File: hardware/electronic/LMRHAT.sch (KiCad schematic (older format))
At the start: 17 parts, among them J1 Speaker Connector, J2 Serial, J5 RPi Expansion Connector, U1 MAX98357AETE+T, U9 SPH0645LM4H-B

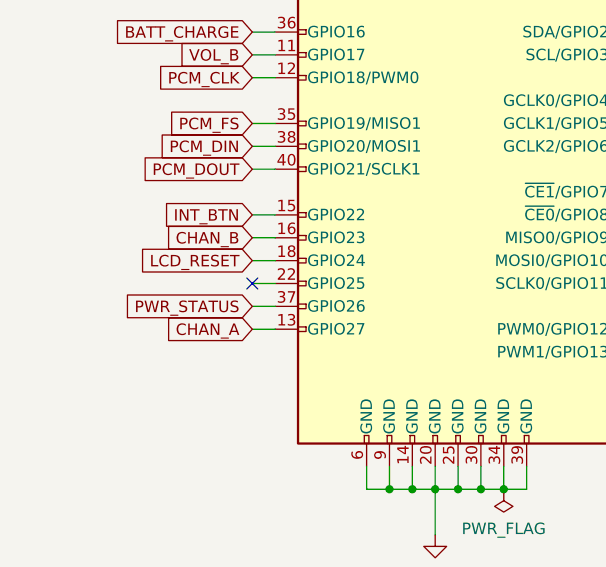
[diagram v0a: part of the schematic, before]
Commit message: Connected power switch to a GPIO and moved the layout for readability
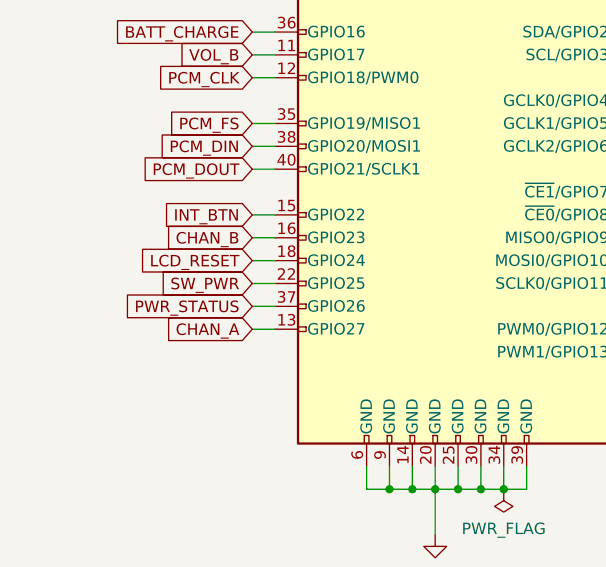
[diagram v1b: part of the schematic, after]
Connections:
- net SW_PWR: now reaches J5.22 (GPIO25)
- no-connect marks 7 -> 6
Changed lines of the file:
@@
 	6700 3500 6900 3500
 NoConn ~ 3500 3500
-NoConn ~ 1700 3200
 $Comp
 L power:PWR_FLAG #FLG0102
@@
 NoConn ~ 3500 2600
 NoConn ~ 3500 2500
+Text GLabel 1700 3200 0    50   Input ~ 0
+SW_PWR
 $EndSCHEMATC

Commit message: Rescued schematic symbols since LMRHAT.lib didn't get saved
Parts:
- MK1, MK2, MK4, MK5, MK6: symbol LMRHAT-rescue:Mounting_Hole-Mechanical -> LMRHAT-rescue:Mounting_Hole-Mechanical-LMRHAT-rescue
- U1: symbol LMRHAT:MAX98357AETE+T -> LMRHAT-rescue:MAX98357AETE+T-LMRHAT
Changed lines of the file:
@@
 $EndDescr
 $Comp
-L LMRHAT-rescue:Mounting_Hole-Mechanical MK1
+L LMRHAT-rescue:Mounting_Hole-Mechanical-LMRHAT-rescue MK1
 U 1 1 5834FB2E
 P 750 6050
@@
 $EndComp
 $Comp
-L LMRHAT-rescue:Mounting_Hole-Mechanical MK2
+L LMRHAT-rescue:Mounting_Hole-Mechanical-LMRHAT-rescue MK2
 U 1 1 5834FC19
 P 750 6250
@@
 $EndComp
 $Comp
-L LMRHAT-rescue:Mounting_Hole-Mechanical MK4
+L LMRHAT-rescue:Mounting_Hole-Mechanical-LMRHAT-rescue MK4
 U 1 1 5834FC4F
 P 1200 6250
@@
 	2300 4100 2400 4100
 $Comp
-L LMRHAT:GND #PWR0142
+L LMRHAT-rescue:GND-LMRHAT #PWR0142
 U 1 1 5C81337F
 P 2500 4300
@@
 Connection ~ 2800 1300
 $Comp
-L LMRHAT:+Vopt #PWR0143
+L LMRHAT-rescue:+Vopt-LMRHAT #PWR0143
 U 1 1 5C916BC8
 P 2400 1200
@@
 $EndComp
 $Comp
-L LMRHAT:+3.3V #PWR0144
+L LMRHAT-rescue:+3.3V-LMRHAT #PWR0144
 U 1 1 5C916CAE
 P 2800 1200
@@
 $EndComp
 $Comp
-L LMRHAT:GND #PWR0101
+L LMRHAT-rescue:GND-LMRHAT #PWR0101
 U 1 1 5C9E3D74
 P 4100 3200
@@
 $EndSheet
 $Comp
-L LMRHAT:MAX98357AETE+T U1
+L LMRHAT-rescue:MAX98357AETE+T-LMRHAT U1
 U 1 1 5C1DD312
 P 7650 2250
@@
 	7100 2500 7050 2500
 $Comp
-L LMRHAT:GND #PWR0102
+L LMRHAT-rescue:GND-LMRHAT #PWR0102
 U 1 1 5C1DD31D
 P 8300 2700
@@
 	6900 2100 7100 2100
 $Comp
-L LMRHAT:GND #PWR0103
+L LMRHAT-rescue:GND-LMRHAT #PWR0103
 U 1 1 5C1DD324
 P 6900 2200
@@
 Connection ~ 6500 2500
 $Comp
-L LMRHAT:GND #PWR0104
+L LMRHAT-rescue:GND-LMRHAT #PWR0104
 U 1 1 5C1DD345
 P 6500 2950
@@
 $EndComp
 $Comp
-L LMRHAT:GND #PWR0105
+L LMRHAT-rescue:GND-LMRHAT #PWR0105
 U 1 1 5C1DD34B
 P 6900 2950
@@
 PCM_CLK
 $Comp
-L LMRHAT:GND #PWR0106
+L LMRHAT-rescue:GND-LMRHAT #PWR0106
 U 1 1 5C1DD370
 P 8300 3950
@@
 	8550 3600 8300 3600
 $Comp
-L LMRHAT:GND #PWR0107
+L LMRHAT-rescue:GND-LMRHAT #PWR0107
 U 1 1 5C1DD379
 P 6800 4150
@@
 $EndComp
 $Comp
-L LMRHAT:GND #PWR0108
+L LMRHAT-rescue:GND-LMRHAT #PWR0108
 U 1 1 5C1DD3AB
 P 9150 3950
@@
 $EndComp
 $Comp
-L LMRHAT:GND #PWR0109
+L LMRHAT-rescue:GND-LMRHAT #PWR0109
 U 1 1 5C1DD3B1
 P 9550 3950
@@
 $EndComp
 $Comp
-L LMRHAT-rescue:Mounting_Hole-Mechanical MK5
+L LMRHAT-rescue:Mounting_Hole-Mechanical-LMRHAT-rescue MK5
 U 1 1 5C2B2A26
 P 750 6450
@@
 $EndComp
 $Comp
-L LMRHAT-rescue:Mounting_Hole-Mechanical MK6
+L LMRHAT-rescue:Mounting_Hole-Mechanical-LMRHAT-rescue MK6
 U 1 1 5C2B2A66
 P 1200 6450

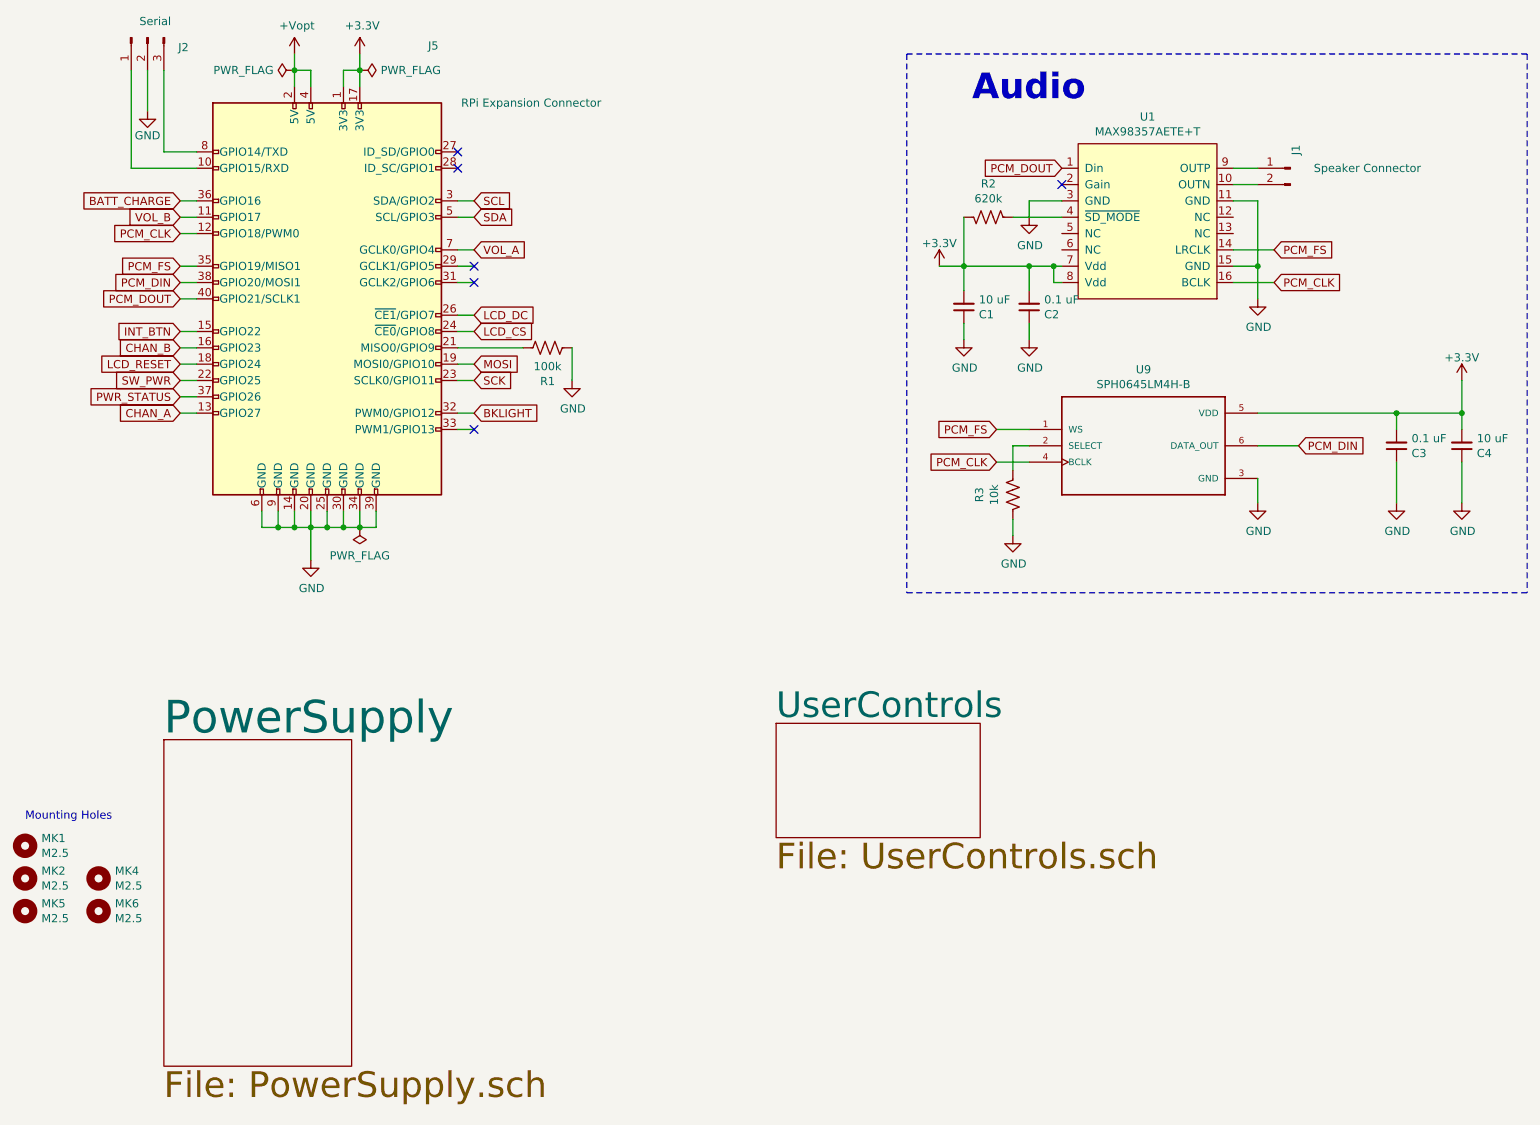
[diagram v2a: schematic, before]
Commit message: Updated layout and schematic to match board dimensions of 50x80mm
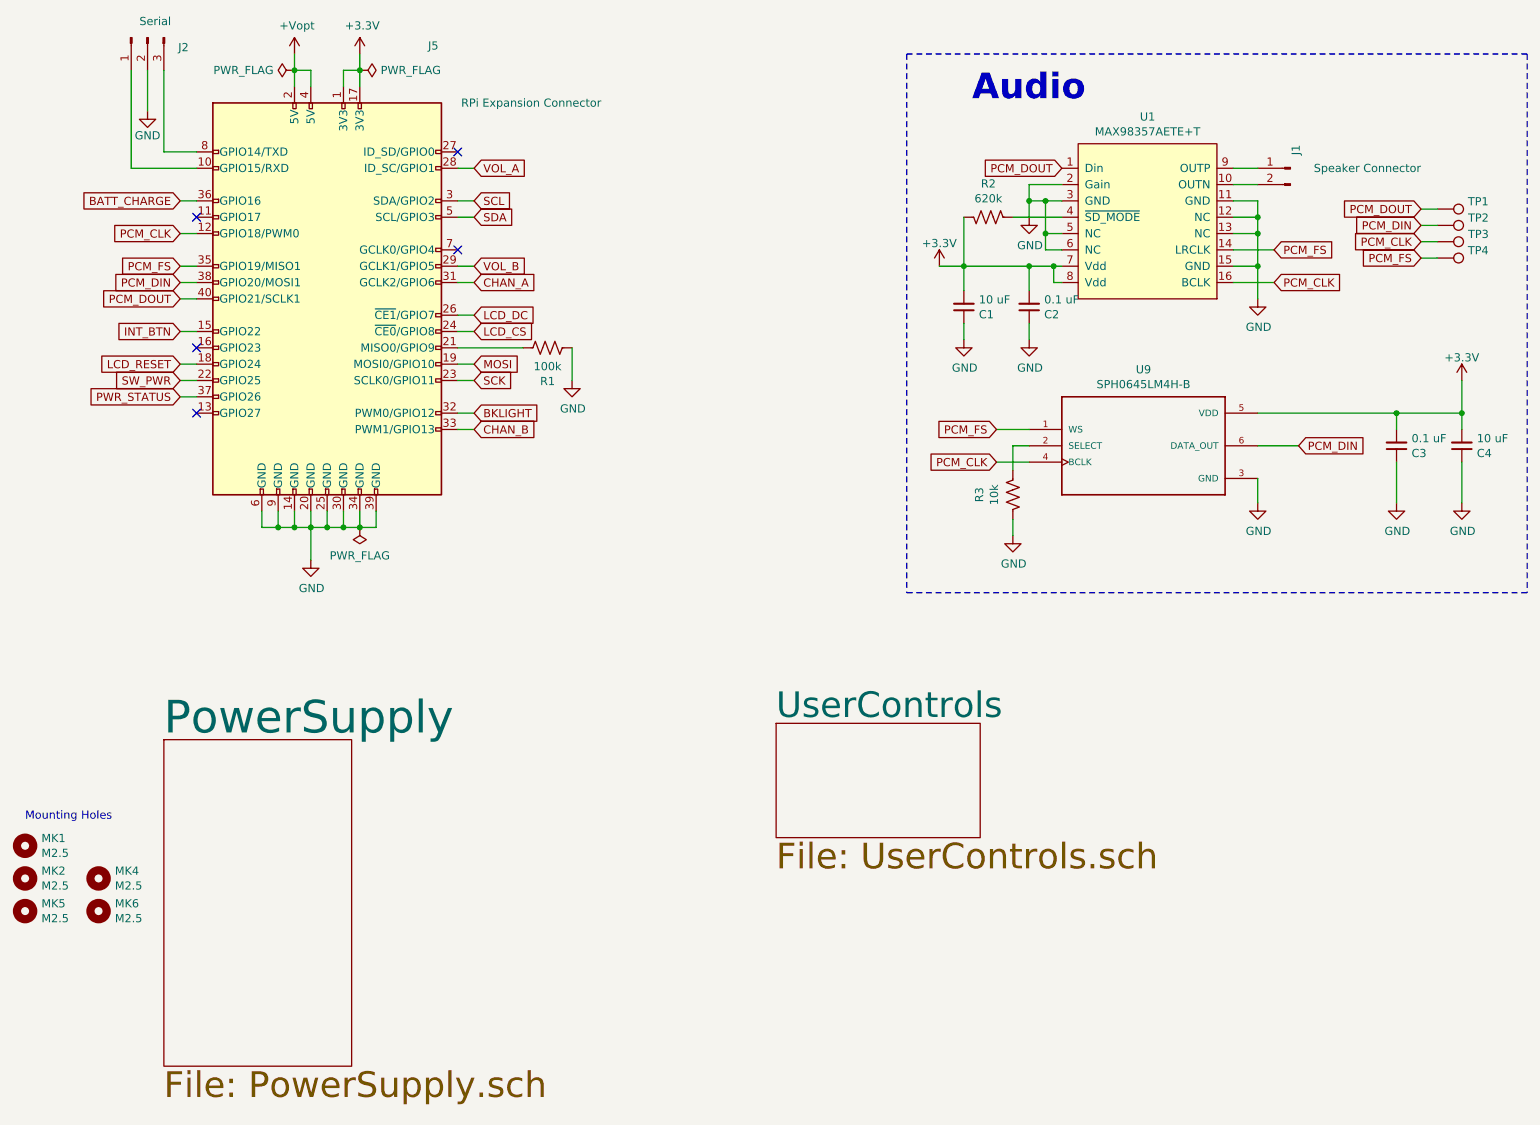
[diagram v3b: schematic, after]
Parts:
- added TP1, TP2, TP3, TP4: (no value), TestPoint:TestPoint_Pad_D1.0mm, symbol Connector:TestPoint
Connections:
- net CHAN_A: now also J5.31 (GCLK2/GPIO6); no longer J5.13 (GPIO27)
- net CHAN_B: now also J5.33 (PWM1/GPIO13); no longer J5.16 (GPIO23)
- net GND: now also U1.12 (NC), U1.13 (NC), U1.2 (Gain), U1.5 (NC), U1.6 (NC)
- net PCM_CLK: now also TP3.1
- net PCM_DIN: now also TP2.1
- net PCM_DOUT: now also TP1.1
- net PCM_FS: now also TP4.1
- net VOL_A: now also J5.28 (ID_SC/GPIO1); no longer J5.7 (GCLK0/GPIO4)
- net VOL_B: now also J5.29 (GCLK1/GPIO5); no longer J5.11 (GPIO17)
- no-connect marks 6 -> 5
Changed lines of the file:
@@
 Text GLabel 3500 2900 2    50   Input ~ 0
 LCD_CS
-Text GLabel 1700 3400 0    50   Input ~ 0
+Text GLabel 3500 2600 2    50   Input ~ 0
 CHAN_A
-Text GLabel 1700 3000 0    50   Input ~ 0
+Text GLabel 3500 3500 2    50   Input ~ 0
 CHAN_B
-Text GLabel 3500 2400 2    50   Input ~ 0
+Text GLabel 3500 1900 2    50   Input ~ 0
 VOL_A
-Text GLabel 1700 2200 0    50   Input ~ 0
+Text GLabel 3500 2500 2    50   Input ~ 0
 VOL_B
 Text GLabel 1700 2900 0    50   Input ~ 0
@@
 Wire Wire Line
 	1400 1900 1400 1300
-NoConn ~ 3400 1900
+NoConn ~ 1800 2200
 NoConn ~ 3400 1800
 Wire Wire Line
@@
 	1700 2900 1800 2900
 Wire Wire Line
-	1700 3000 1800 3000
-Wire Wire Line
 	1700 3100 1800 3100
 Wire Wire Line
@@
 Wire Wire Line
 	1700 3300 1800 3300
-Wire Wire Line
-	1700 3400 1800 3400
 Wire Wire Line
 	2200 4000 2200 4100
@@
 	3400 3500 3500 3500
 Wire Wire Line
-	3400 2400 3500 2400
-Wire Wire Line
 	3400 2500 3500 2500
 Wire Wire Line
@@
 Wire Wire Line
 	1700 2100 1800 2100
-Wire Wire Line
-	1700 2200 1800 2200
 Wire Wire Line
 	2400 1400 2400 1300
@@
 $EndComp
 Wire Wire Line
-	6900 2100 7100 2100
+	6900 2100 7000 2100
 $Comp
 L LMRHAT-rescue:GND-LMRHAT #PWR0103
@@
 	6800 4050 6800 4150
 Wire Wire Line
-	8300 2100 8300 2500
+	8300 2100 8300 2200
 Wire Wire Line
 	7100 2600 7050 2600
@@
 Wire Wire Line
 	6700 3500 6900 3500
-NoConn ~ 3500 3500
+NoConn ~ 1800 3000
 $Comp
 L power:PWR_FLAG #FLG0102
@@
 Wire Wire Line
 	6800 2200 7100 2200
-NoConn ~ 7100 2000
 $Comp
 L Device:R_US R2
@@
 Text GLabel 1700 3300 0    50   Input ~ 0
 PWR_STATUS
-NoConn ~ 3500 2600
-NoConn ~ 3500 2500
+NoConn ~ 1800 3400
+NoConn ~ 3400 2400
 Text GLabel 1700 3200 0    50   Input ~ 0
 SW_PWR
+Wire Wire Line
+	3500 1900 3400 1900
+Wire Wire Line
+	6900 2100 6900 2000
+Wire Wire Line
+	6900 2000 7100 2000
+Connection ~ 6900 2100
+Wire Wire Line
+	7100 2300 7000 2300
+Wire Wire Line
+	7000 2300 7000 2100
+Connection ~ 7000 2100
+Wire Wire Line
+	7000 2100 7100 2100
+Wire Wire Line
+	7100 2400 7000 2400
+Wire Wire Line
+	7000 2400 7000 2300
+Connection ~ 7000 2300
+Wire Wire Line
+	8150 2200 8300 2200
+Connection ~ 8300 2200
+Wire Wire Line
+	8300 2200 8300 2300
+Wire Wire Line
+	8150 2300 8300 2300
+Connection ~ 8300 2300
+Wire Wire Line
+	8300 2300 8300 2500
+Text GLabel 9300 2150 0    50   Input ~ 0
+PCM_DOUT
+Text GLabel 9300 2250 0    50   Input ~ 0
+PCM_DIN
+Text GLabel 9300 2350 0    50   Input ~ 0
+PCM_CLK
+Text GLabel 9300 2450 0    50   Input ~ 0
+PCM_FS
+$Comp
+L Connector:TestPoint TP1
+U 1 1 5C569EF1
+P 9400 2150
+F 0 "TP1" V 9354 2337 50  0000 L CNN
+F 1 " " V 9445 2337 50  0000 L CNN
+F 2 "TestPoint:TestPoint_Pad_D1.0mm" H 9600 2150 50  0001 C CNN
+F 3 "~" H 9600 2150 50  0001 C CNN
+	1    9400 2150
+	0    1    1    0
+$EndComp
+$Comp
+L Connector:TestPoint TP2
+U 1 1 5C569FDC
+P 9400 2250
+F 0 "TP2" V 9354 2438 50  0000 L CNN
+F 1 " " V 9445 2438 50  0000 L CNN
+F 2 "TestPoint:TestPoint_Pad_D1.0mm" H 9600 2250 50  0001 C CNN
+F 3 "~" H 9600 2250 50  0001 C CNN
+	1    9400 2250
+	0    1    1    0
+$EndComp
+$Comp
+L Connector:TestPoint TP3
+U 1 1 5C56A065
+P 9400 2350
+F 0 "TP3" V 9354 2538 50  0000 L CNN
+F 1 " " V 9445 2538 50  0000 L CNN
+F 2 "TestPoint:TestPoint_Pad_D1.0mm" H 9600 2350 50  0001 C CNN
+F 3 "~" H 9600 2350 50  0001 C CNN
+	1    9400 2350
+	0    1    1    0
+$EndComp
+$Comp
+L Connector:TestPoint TP4
+U 1 1 5C56A0EE
+P 9400 2450
+F 0 "TP4" V 9354 2637 50  0000 L CNN
+F 1 " " V 9445 2637 50  0000 L CNN
+F 2 "TestPoint:TestPoint_Pad_D1.0mm" H 9600 2450 50  0001 C CNN
+F 3 "~" H 9600 2450 50  0001 C CNN
+	1    9400 2450
+	0    1    1    0
+$EndComp
+Wire Wire Line
+	9400 2450 9300 2450
+Wire Wire Line
+	9300 2350 9400 2350
+Wire Wire Line
+	9400 2250 9300 2250
+Wire Wire Line
+	9300 2150 9400 2150
 $EndSCHEMATC
